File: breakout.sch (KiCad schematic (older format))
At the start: 33 parts, among them CON1 SD_Card, CON2 USB-MICRO-AB, P2 CONN_01X40, P3 CONN_01X40, P4 CONN_01X40, P5 A-DF-09-A/KG-T4S, SW1 SW_PUSH

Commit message: removed unecessary fuse, checked footprints
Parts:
- removed F1: 0603SFV300F/32-2, SMD_Packages:SMD-1206_Pol, symbol FUSE_SMD
- removed GND1: CONN_01X02, Terminal_Blocks:TerminalBlock_WAGO-236_2Stift_RM5mm_1pol, symbol CONN_01X02
- C1: footprint Capacitors_SMD:C_0201 -> Capacitors_Elko_ThroughHole:Elko_vert_25x12.5mm_RM5_CopperClear
- C5, C6: footprint Capacitors_SMD:C_0402 -> Capacitors_SMD:C_0805
- D1: value D_Small -> B340; footprint Diodes_ThroughHole:Diode_DO-35_SOD27_Horizontal_RM10 -> Diodes_SMD:Diode-SMC_Standard
- L1: footprint SMD_Packages:SMD-1206_Pol -> Choke_SMD:Choke_SMD_12x12mm_h8mm
- L2: footprint Capacitors_SMD:C_0201 -> Capacitors_SMD:C_0805
- POWER1: footprint Terminal_Blocks:TerminalBlock_WAGO-236_2Stift_RM5mm_1pol -> Custom Footprints:1792863
- SW1: footprint (none) -> Custom Footprints:1825910-7
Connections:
- wire segments 70 -> 66
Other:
- moved on the sheet: POWER1
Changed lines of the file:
@@
 L CONN_01X02 POWER1
 U 1 1 55FF7251
-P 2450 750
-F 0 "POWER1" H 2350 900 50  0000 C CNN
-F 1 "CONN_01X02" V 2550 750 50  0000 C CNN
-F 2 "Terminal_Blocks:TerminalBlock_WAGO-236_2Stift_RM5mm_1pol" H 2450 750 60  0001 C CNN
-F 3 "" H 2450 750 60  0000 C CNN
-	1    2450 750
-	1    0    0    -1
+P 1400 800
+F 0 "POWER1" H 1250 1000 50  0000 C CNN
+F 1 "CONN_01X02" V 1500 800 50  0000 C CNN
+F 2 "Custom Footprints:1792863" H 1400 800 60  0001 C CNN
+F 3 "" H 1400 800 60  0000 C CNN
+	1    1400 800
+	-1   0    0    -1
 $EndComp
 $Comp
@@
 F 0 "L1" V 1750 2300 50  0000 L CNN
 F 1 "22uH" V 1600 2250 50  0000 L CNN
-F 2 "SMD_Packages:SMD-1206_Pol" H 1650 2350 60  0001 C CNN
+F 2 "Choke_SMD:Choke_SMD_12x12mm_h8mm" H 1650 2350 60  0001 C CNN
 F 3 "" H 1650 2350 60  0000 C CNN
 	1    1650 2350
@@
 F 0 "C1" H 950 2350 50  0000 L CNN
 F 1 "470uF" H 800 2450 50  0000 L CNN
-F 2 "Capacitors_SMD:C_0201" H 1100 2450 60  0001 C CNN
+F 2 "Capacitors_Elko_ThroughHole:Elko_vert_25x12.5mm_RM5_CopperClear" H 1100 2450 60  0001 C CNN
 F 3 "" H 1100 2450 60  0000 C CNN
 	1    1100 2450
@@
 P 1450 2450
 F 0 "D1" V 1400 2530 50  0000 L CNN
-F 1 "D_Small" V 1350 2100 50  0000 L CNN
-F 2 "Diodes_ThroughHole:Diode_DO-35_SOD27_Horizontal_RM10" V 1450 2450 60  0001 C CNN
+F 1 "B340" V 1350 2200 50  0000 L CNN
+F 2 "Diodes_SMD:Diode-SMC_Standard" V 1450 2450 60  0001 C CNN
 F 3 "" V 1450 2450 60  0000 C CNN
 	1    1450 2450
@@
 	1    0    0    -1
 $EndComp
-$Comp
-L CONN_01X02 GND1
-U 1 1 561CE1C4
-P 1450 750
-F 0 "GND1" H 1350 900 50  0000 C CNN
-F 1 "CONN_01X02" V 1550 750 50  0000 C CNN
-F 2 "Terminal_Blocks:TerminalBlock_WAGO-236_2Stift_RM5mm_1pol" H 1450 750 60  0001 C CNN
-F 3 "" H 1450 750 60  0000 C CNN
-	1    1450 750
-	-1   0    0    1
-$EndComp
-Text Label 1700 750  0    60   ~ 0
-GND
-Text Label 2200 750  2    60   ~ 0
+Text Label 1600 850  0    60   ~ 0
+GND
+Text Label 1600 750  0    60   ~ 0
 RAIL
 Text Label 3900 5550 2    60   ~ 0
@@
 F 0 "L2" H 2650 4200 50  0000 C CNN
 F 1 "4.7uH" H 2650 4050 50  0000 C CNN
-F 2 "Capacitors_SMD:C_0201" H 2650 4100 60  0001 C CNN
+F 2 "Capacitors_SMD:C_0805" H 2650 4100 60  0001 C CNN
 F 3 "" H 2650 4100 60  0000 C CNN
 	1    2650 4100
@@
 F 0 "C5" H 2900 4100 50  0000 L CNN
 F 1 "22uF" H 3100 4100 50  0000 L CNN
-F 2 "Capacitors_SMD:C_0402" H 3050 4200 60  0001 C CNN
+F 2 "Capacitors_SMD:C_0805" H 3050 4200 60  0001 C CNN
 F 3 "" H 3050 4200 60  0000 C CNN
 	1    3050 4200
@@
 F 0 "C6" H 3400 3900 50  0000 L CNN
 F 1 "22uF" H 3100 3900 50  0000 L CNN
-F 2 "Capacitors_SMD:C_0402" H 3350 4000 60  0001 C CNN
+F 2 "Capacitors_SMD:C_0805" H 3350 4000 60  0001 C CNN
 F 3 "" H 3350 4000 60  0000 C CNN
 	1    3350 4000
@@
 F 0 "SW1" H 1400 8360 50  0000 C CNN
 F 1 "SW_PUSH" H 1250 8170 50  0000 C CNN
-F 2 "" H 1250 8250 60  0001 C CNN
+F 2 "Custom Footprints:1825910-7" H 1250 8250 60  0001 C CNN
 F 3 "" H 1250 8250 60  0000 C CNN
 	1    1250 8250
@@
 GND
 $Comp
-L FUSE_SMD F1
-U 1 1 561C33B9
-P 850 2150
-F 0 "F1" H 810 2210 50  0000 L CNN
-F 1 "0603SFV300F/32-2" H 300 2000 50  0000 L CNN
-F 2 "SMD_Packages:SMD-1206_Pol" H 850 2150 60  0001 C CNN
-F 3 "" H 850 2150 60  0000 C CNN
-	1    850  2150
-	0    1    1    0
-$EndComp
-$Comp
 L GND #PWR015
 U 1 1 562880B7
@@
 	850  2350 1300 2350
 Wire Wire Line
-	850  2350 850  2250
+	850  2350 850  2050
 Wire Wire Line
 	1750 2350 2150 2350
 Wire Wire Line
 	850  950  900  950
-Wire Wire Line
-	1650 700  1650 800
-Wire Wire Line
-	1650 750  1700 750
-Connection ~ 1650 750
-Wire Wire Line
-	2250 700  2250 800
-Wire Wire Line
-	2250 750  2200 750
-Connection ~ 2250 750
 Connection ~ 2000 2350
 Wire Wire Line

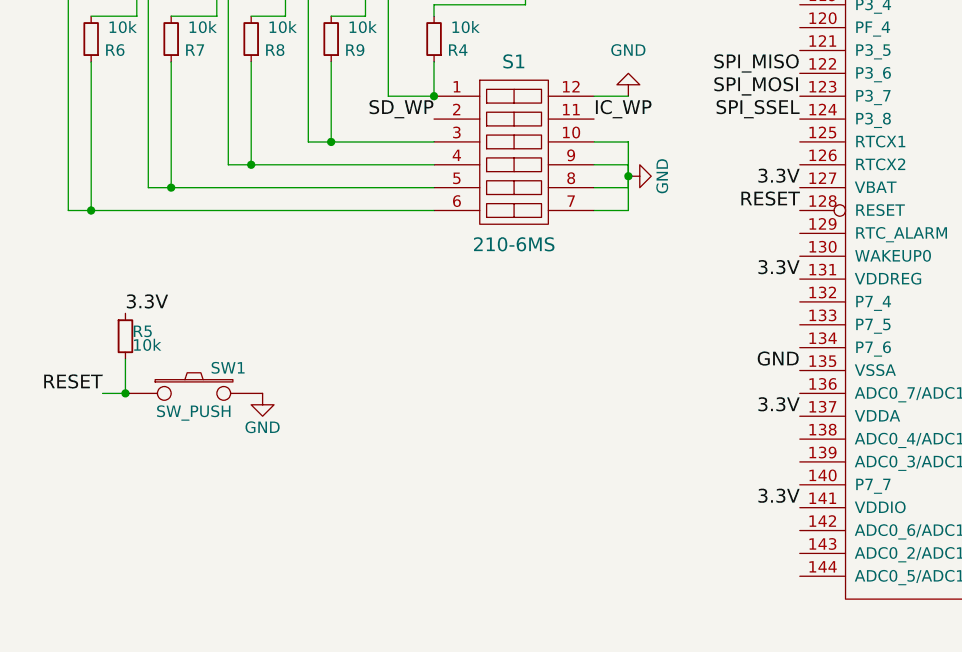
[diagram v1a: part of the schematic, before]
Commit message: added battery to schematic
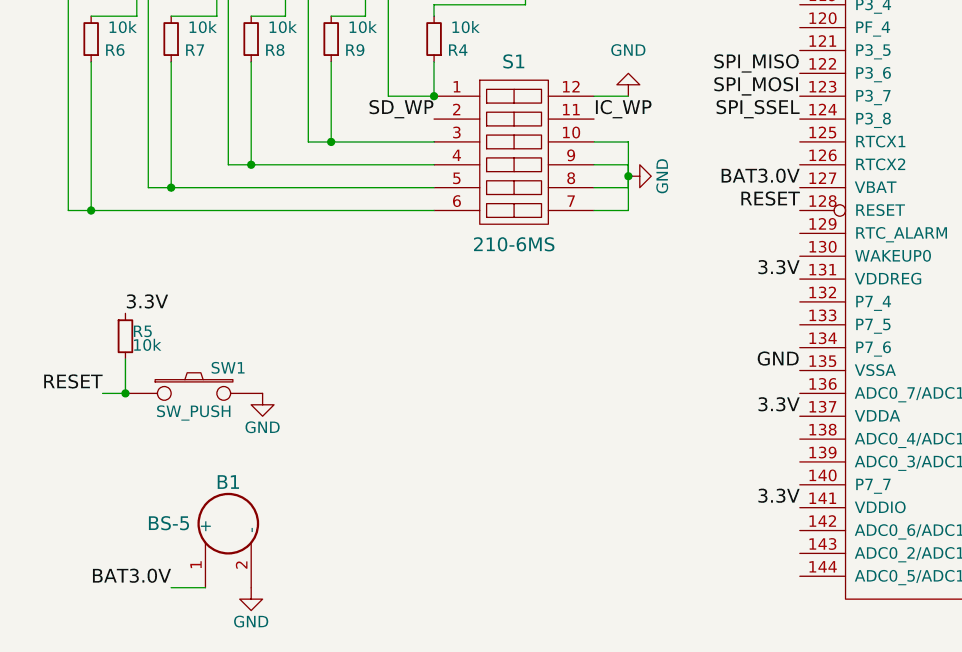
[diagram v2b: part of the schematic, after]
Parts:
- added B1: BS-5, Custom Footprints:BS-5, symbol BS-5
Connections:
- net 3.3V: no longer CPU1.127 (VBAT)
- net GND: now also B1.2 (-)
- new net BAT3.0V: B1.1 (+), CPU1.127 (VBAT)
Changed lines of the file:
@@
 LIBS:cts
 LIBS:molex
+LIBS:mpd
 LIBS:breakout-cache
 EELAYER 25 0
@@
 3.3V
 Text Label 3900 7350 2    60   ~ 0
-3.3V
+BAT3.0V
 Text Label 3900 8350 2    60   ~ 0
 3.3V
@@
 	950  8250 850  8250
 Connection ~ 950  8250
+$Comp
+L BS-5 B1
+U 1 1 563D3D9D
+P 1400 8950
+F 0 "B1" H 1400 9260 60  0000 C CNN
+F 1 "BS-5" H 1140 9080 60  0000 C CNN
+F 2 "Custom Footprints:BS-5" H 1400 9080 60  0001 C CNN
+F 3 "" H 1400 9080 60  0000 C CNN
+	1    1400 8950
+	1    0    0    -1
+$EndComp
+Text Label 1150 9100 2    60   ~ 0
+BAT3.0V
+$Comp
+L GND #PWR?
+U 1 1 563D5013
+P 1500 9100
+F 0 "#PWR?" H 1500 8850 50  0001 C CNN
+F 1 "GND" H 1500 8950 50  0000 C CNN
+F 2 "" H 1500 9100 60  0000 C CNN
+F 3 "" H 1500 9100 60  0000 C CNN
+	1    1500 9100
+	1    0    0    -1
+$EndComp
+Wire Wire Line
+	1300 9100 1150 9100
 $EndSCHEMATC

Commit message: fixing net names
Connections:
- net GND: no longer PWR2.14 (PGND), PWR2.15 (PGND), PWR2.17 (PAD)
- net VSW: no longer PWR2.13 (VSW), PWR2.16 (VSW)
- net P6_10: now reaches CPU1.100 (P6_10)
- net P6_11: now reaches CPU1.101 (P6_11)
- net P6_12: now reaches CPU1.103 (P6_12)
- net P2_10: now reaches CPU1.104 (P2_10)
- net P2_11: now reaches CPU1.105 (P2_11)
- net P2_12: now reaches CPU1.106 (P2_12)
- net P2_13: now reaches CPU1.108 (P2_13)
- net P7_0: now reaches CPU1.110 (P7_0)
- net P3_0: now reaches CPU1.112 (P3_0)
- net P7_1: now reaches CPU1.113 (P7_1)
- net P3_1: now reaches CPU1.114 (P3_1)
- net P7_2: now reaches CPU1.115 (P7_2)
- net P3_2: now reaches CPU1.116 (P3_2)
- net P7_3: now reaches CPU1.117 (P7_3)
- net P3_4: now reaches CPU1.119 (P3_4)
- net PF_4: now reaches CPU1.120 (PF_4)
- net P3_5: now reaches CPU1.121 (P3_5)
- net RTCX1: now reaches CPU1.125 (RTCX1)
- net RTCX2: now reaches CPU1.126 (RTCX2)
- net RTC_ALARM: now reaches CPU1.129 (RTC_ALARM)
- net WAKEUP0: now reaches CPU1.130 (WAKEUP0)
- net P7_4: now reaches CPU1.132 (P7_4)
- net P7_5: now reaches CPU1.133 (P7_5)
- net P7_6: now reaches CPU1.134 (P7_6)
- net ADC0_7: now reaches CPU1.136 (ADC0_7/ADC1_7)
- net ADC0_4: now reaches CPU1.138 (ADC0_4/ADC1_4)
- net ADC0_3: now reaches CPU1.139 (ADC0_3/ADC1_3)
- net P7_7: now reaches CPU1.140 (P7_7)
- net ADC0_6: now reaches CPU1.142 (ADC0_6/ADC1_6)
- net ADC0_2: now reaches CPU1.143 (ADC0_2/ADC1_2)
- net ADC0_5: now reaches CPU1.144 (ADC0_5/ADC1_5)
- net USB0_D+: now reaches CON2.3 (D+), CPU1.18 (USB0_DP)
- net USB0_D-: now reaches CON2.2 (D-), CPU1.20 (USB0_DM)
- net USB0_ID: now reaches CON2.4 (ID), CPU1.22 (USB0_ID)
- net P6_0: now reaches CPU1.73 (P6_0)
- net P6_1: now reaches CPU1.74 (P6_1)
- net P6_2: now reaches CPU1.78 (P6_2)
- net P6_3: now reaches CPU1.79 (P6_3)
- net P6_4: now reaches CPU1.80 (P6_4)
- net P6_5: now reaches CPU1.82 (P6_5)
- net P6_6: now reaches CPU1.83 (P6_6)
- net P2_2: now reaches CPU1.84 (P2_2)
- net P6_7: now reaches CPU1.85 (P6_7)
- net P6_8: now reaches CPU1.86 (P6_8)
- net P2_4: now reaches CPU1.88 (P2_4)
- net USB1_D+: now reaches CPU1.89 (USB1_DP)
- net USB1_D-: now reaches CPU1.90 (USB1_DM)
- net P2_5: now reaches CPU1.91 (P2_5)
- net I2C0_SCL: now reaches CPU1.92 (I2C0_SCL)
- net I2C0_SDA: now reaches CPU1.93 (I2C0_SDA)
- net P2_6: now reaches CPU1.95 (P2_6)
- net P6_9: now reaches CPU1.97 (P6_9)
- net CLK2: now reaches CPU1.99 (CLK2)
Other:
- moved on the sheet: B1, C3, C4, C5, C6, CON1, CON2, CPU1, G1, L2, P2, P3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

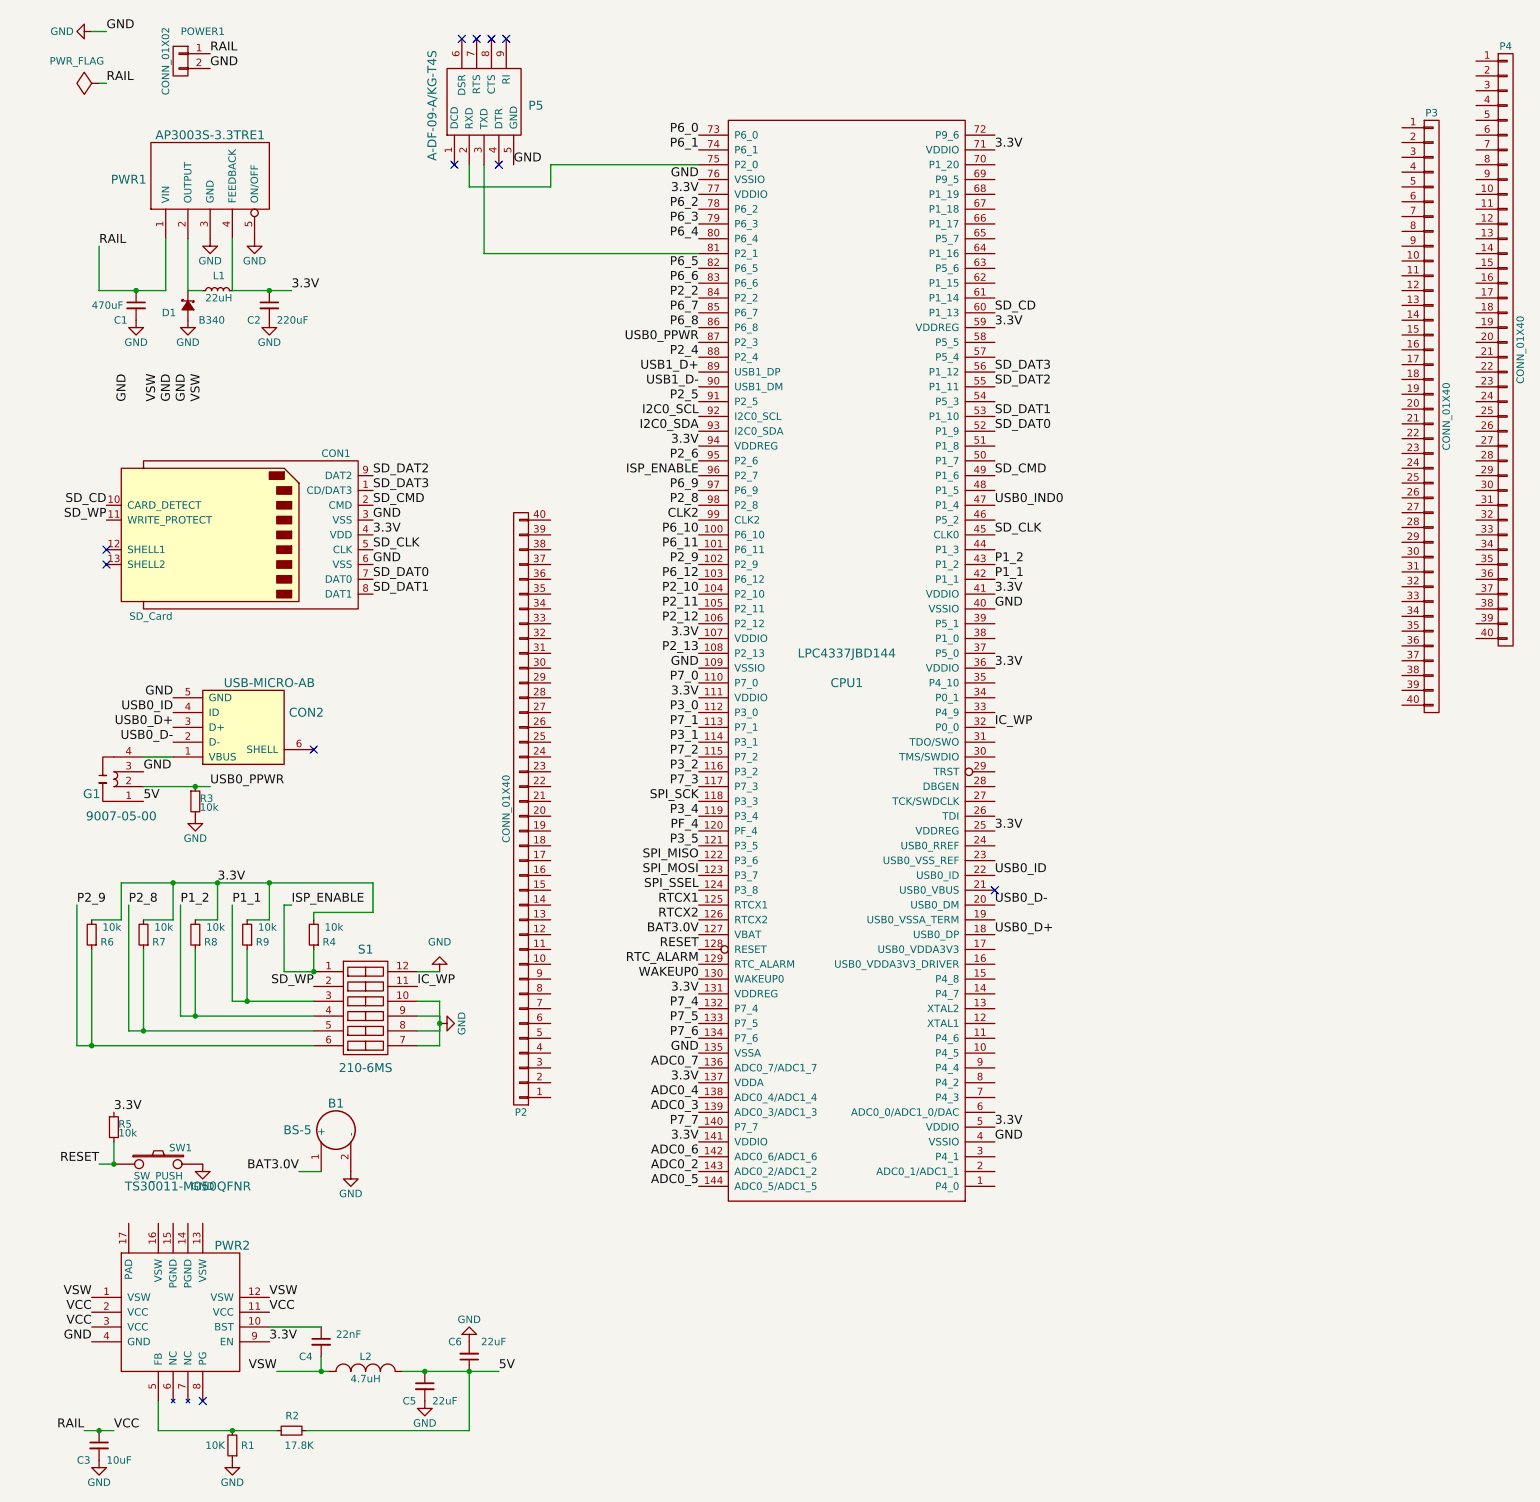
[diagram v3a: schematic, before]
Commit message: added more nets
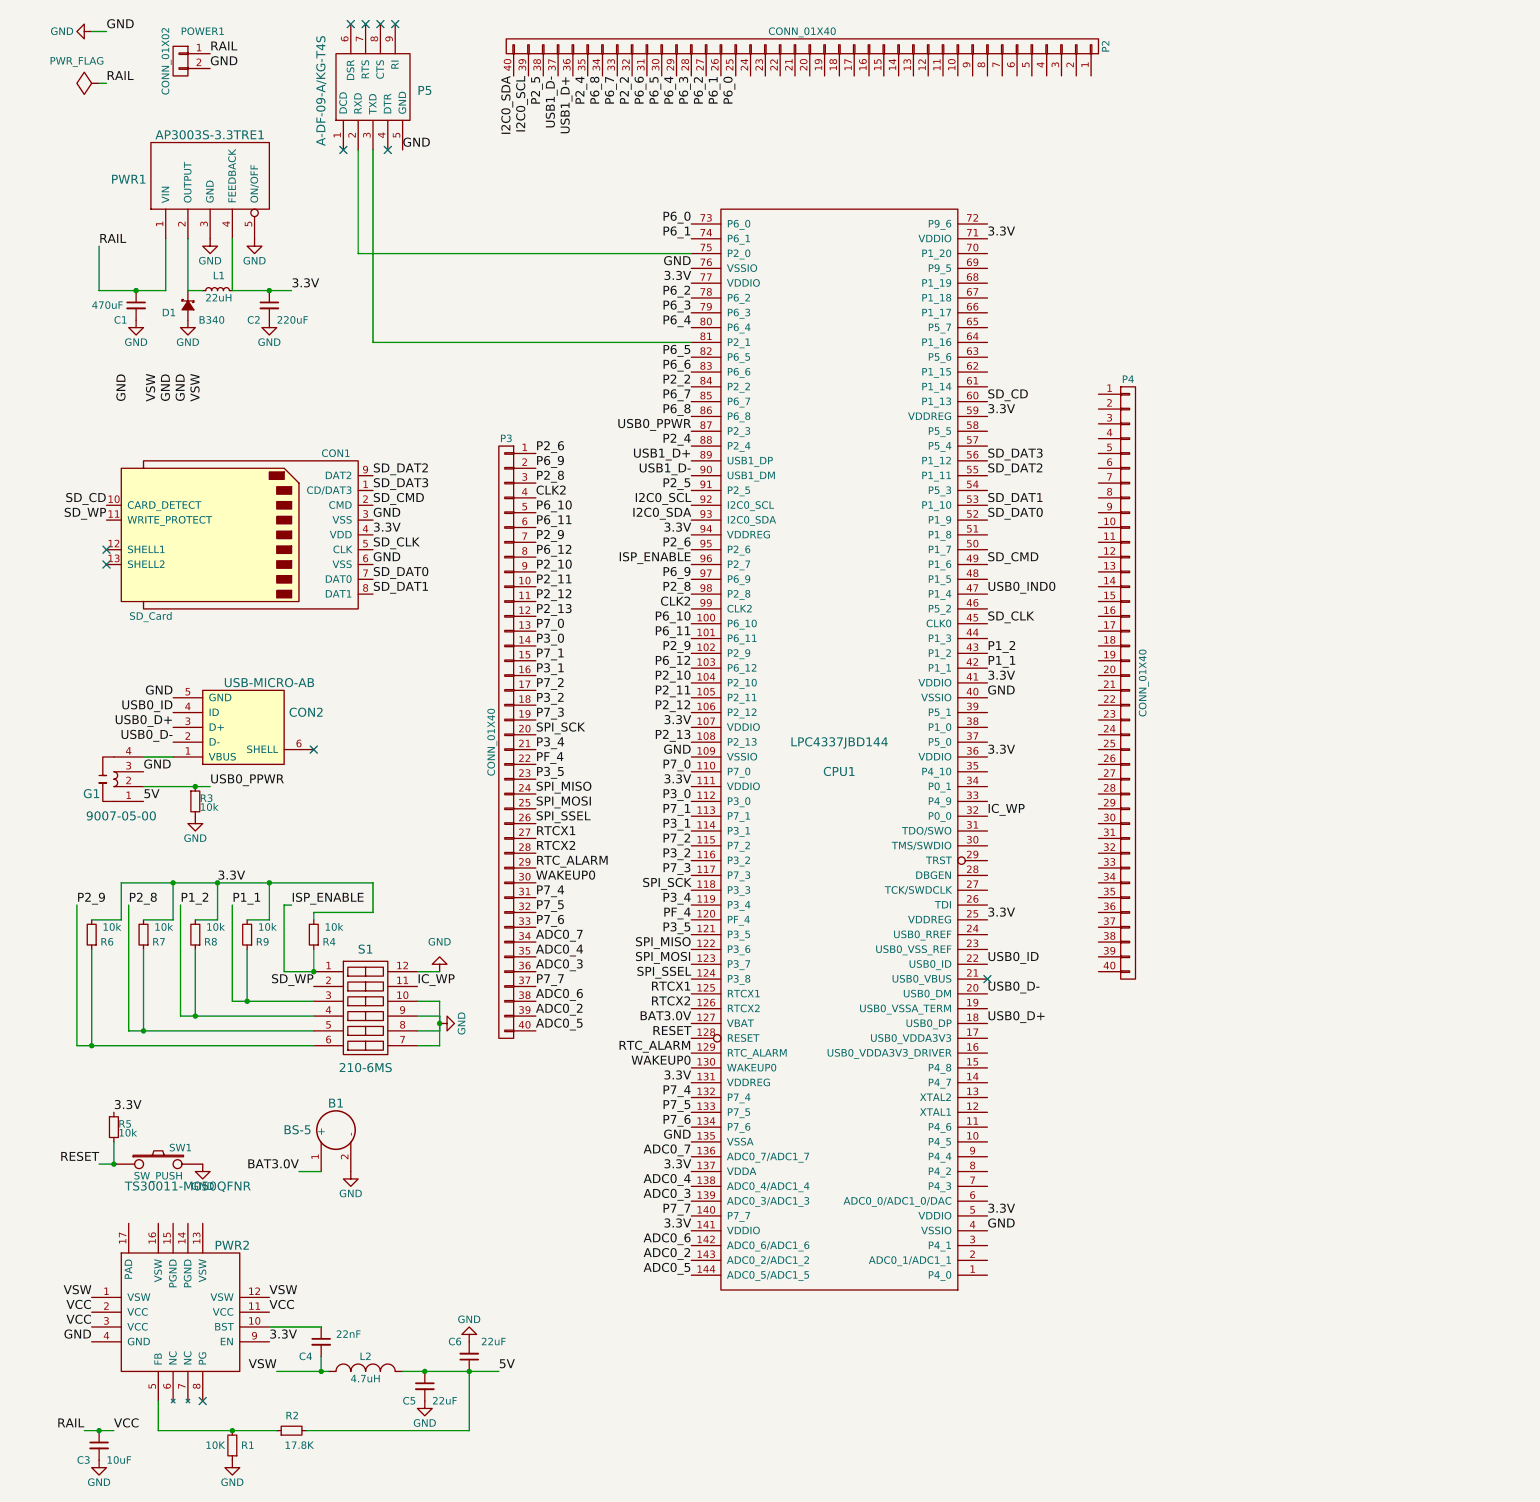
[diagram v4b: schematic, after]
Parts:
- renumbered P3 to P2, P2 to P3
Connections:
- net ADC0_2: now also P3.39 (P39)
- net ADC0_3: now also P3.36 (P36)
- net ADC0_4: now also P3.35 (P35)
- net ADC0_5: now also P3.40 (P40)
- net ADC0_6: now also P3.38 (P38)
- net ADC0_7: now also P3.34 (P34)
- net CLK2: now also P3.4 (P4)
- net I2C0_SCL: now also P2.39 (P39)
- net I2C0_SDA: now also P2.40 (P40)
- net P2_10: now also P3.9 (P9)
- net P2_11: now also P3.10 (P10)
- net P2_12: now also P3.11 (P11)
- net P2_13: now also P3.12 (P12)
- net P2_2: now also P2.32 (P32)
- net P2_4: now also P2.35 (P35)
- net P2_5: now also P2.38 (P38)
- net P2_6: now also P3.1 (P1)
- net P2_8: now also P3.3 (P3)
- net P2_9: now also P3.7 (P7)
- net P3_0: now also P3.14 (P14)
- net P3_1: now also P3.16 (P16)
- net P3_2: now also P3.18 (P18)
- net P3_4: now also P3.21 (P21)
- net P3_5: now also P3.23 (P23)
- net P6_0: now also P2.25 (P25)
- net P6_1: now also P2.26 (P26)
- net P6_10: now also P3.5 (P5)
- net P6_11: now also P3.6 (P6)
- net P6_12: now also P3.8 (P8)
- net P6_2: now also P2.27 (P27)
- net P6_3: now also P2.28 (P28)
- net P6_4: now also P2.29 (P29)
- net P6_5: now also P2.30 (P30)
- net P6_6: now also P2.31 (P31)
- net P6_7: now also P2.33 (P33)
- net P6_8: now also P2.34 (P34)
- net P6_9: now also P3.2 (P2)
- net P7_0: now also P3.13 (P13)
- net P7_1: now also P3.15 (P15)
- net P7_2: now also P3.17 (P17)
- net P7_3: now also P3.19 (P19)
- net P7_4: now also P3.31 (P31)
- net P7_5: now also P3.32 (P32)
- net P7_6: now also P3.33 (P33)
- net P7_7: now also P3.37 (P37)
- net PF_4: now also P3.22 (P22)
- net RTCX1: now also P3.27 (P27)
- net RTCX2: now also P3.28 (P28)
- net RTC_ALARM: now also P3.29 (P29)
- net SPI_MISO: now also P3.24 (P24)
- net SPI_MOSI: now also P3.25 (P25)
- net SPI_SCK: now also P3.20 (P20)
- net SPI_SSEL: now also P3.26 (P26)
- net USB1_D+: now also P2.36 (P36)
- net USB1_D-: now also P2.37 (P37)
- net WAKEUP0: now also P3.30 (P30)
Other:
- moved on the sheet: CPU1, P2, P3, P4, P5
